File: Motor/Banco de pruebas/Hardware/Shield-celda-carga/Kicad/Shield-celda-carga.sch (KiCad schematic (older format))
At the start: 12 parts, among them J1 Screw_Terminal_01x02, J2 Screw_Terminal_01x03, J3 Conn_01x04, J4 Alimentacion Arduino, K1 Rele 12V-360mW, Q1 BC337, U1 HX711

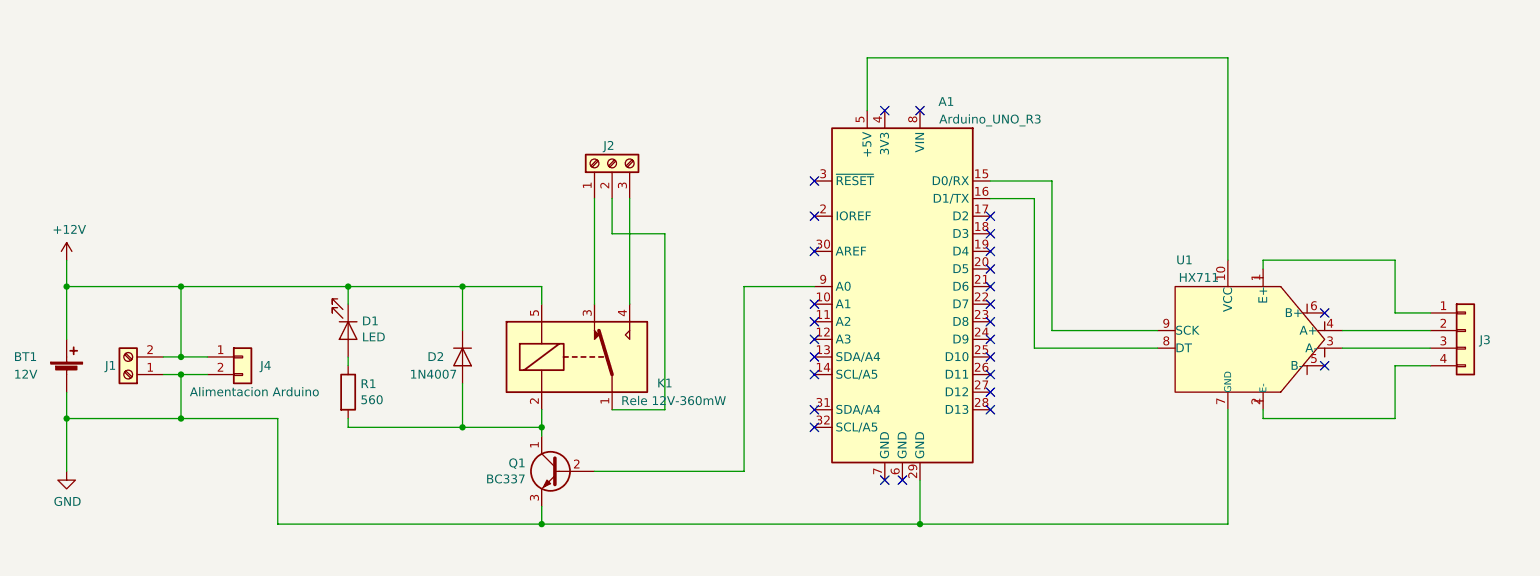
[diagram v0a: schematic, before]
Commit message: Nueva placa Shield-celda-carga
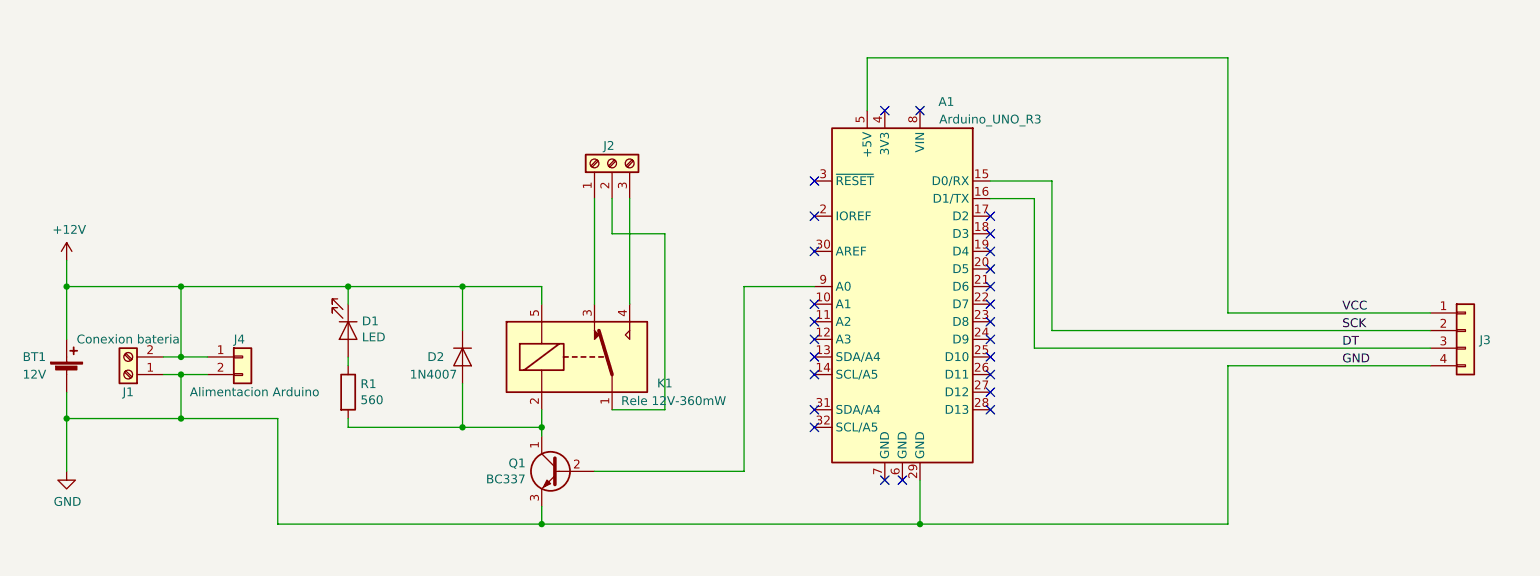
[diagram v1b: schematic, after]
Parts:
- removed U1: HX711, kicad:HX711 module, symbol hx711:HX711
- J1: value Screw_Terminal_01x02 -> Conexion bateria
- J3: footprint Connector_PinHeader_2.54mm:PinHeader_1x05_P2.54mm_Horizontal -> Connector_PinHeader_2.54mm:PinHeader_1x04_P2.54mm_Horizontal
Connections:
- net GND: now also J3.4 (Pin_4)
- net SCK: now reaches A1.15 (D0/RX)
- net SCK: now also J3.2 (Pin_2)
- net DT: now reaches A1.16 (D1/TX)
- net DT: now also J3.3 (Pin_3)
- net VCC: now reaches A1.5 (+5V)
- net VCC: now also J3.1 (Pin_1)
- no-connect marks 28 -> 26
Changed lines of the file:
@@
 $EndComp
-$Comp
-L hx711:HX711 U1
-U 1 1 5E88FDFC
-P 7450 2600
-F 0 "U1" H 7650 3050 50  0000 L CNN
-F 1 "HX711" H 7500 2950 50  0000 L CNN
-F 2 "kicad:HX711 module" H 7500 2950 50  0001 L CNN
-F 3 "http://www.ti.com/lit/ds/symlink/ads1110.pdf" H 7150 2950 50  0001 C CNN
-	1    7450 2600
-	-1   0    0    -1
-$EndComp
-Wire Wire Line
-	7450 3000 7450 3650
-Wire Wire Line
-	7450 2150 7450 1000
 $Comp
 L Connector_Generic:Conn_01x04 J3
@@
 F 0 "J3" H 8880 2496 50  0000 L CNN
 F 1 "Conn_01x04" H 8880 2451 50  0001 L CNN
-F 2 "Connector_PinHeader_2.54mm:PinHeader_1x05_P2.54mm_Horizontal" H 8800 2550 50  0001 C CNN
+F 2 "Connector_PinHeader_2.54mm:PinHeader_1x04_P2.54mm_Horizontal" H 8800 2550 50  0001 C CNN
 F 3 "~" H 8800 2550 50  0001 C CNN
 	1    8800 2550
 	1    0    0    -1
 $EndComp
-Wire Wire Line
-	8100 2550 8600 2550
-Wire Wire Line
-	8600 2650 8100 2650
-Wire Wire Line
-	7650 2200 7650 2150
-Wire Wire Line
-	8400 2450 8600 2450
-Wire Wire Line
-	7650 3000 7650 3050
-Wire Wire Line
-	7650 3050 8400 3050
-Wire Wire Line
-	8400 3050 8400 2750
-Wire Wire Line
-	8400 2750 8600 2750
 $Comp
 L Connector:Screw_Terminal_01x02 J1
 U 1 1 5E898B2F
 P 1200 2800
-F 0 "J1" H 1300 2750 50  0000 C CNN
-F 1 "Screw_Terminal_01x02" H 1118 2566 50  0001 C CNN
+F 0 "J1" H 1200 2900 50  0000 C CNN
+F 1 "Conexion bateria" H 1200 2600 50  0000 C CNN
 F 2 "TerminalBlock_Altech:Altech_AK300_1x02_P5.00mm_45-Degree" H 1200 2800 50  0001 C CNN
 F 3 "~" H 1200 2800 50  0001 C CNN
@@
 U 1 1 5E899902
 P 850 2800
-F 0 "BT1" H 550 2900 50  0000 L CNN
-F 1 "12V" H 550 2800 50  0000 L CNN
+F 0 "BT1" H 600 2900 50  0000 L CNN
+F 1 "12V" H 600 2800 50  0000 L CNN
 F 2 "" V 850 2860 50  0001 C CNN
 F 3 "~" V 850 2860 50  0001 C CNN
@@
 	5400 1000 5400 1300
 Wire Wire Line
-	6350 2650 6350 1800
-Wire Wire Line
 	6350 1800 6100 1800
 Wire Wire Line
-	6350 2650 7050 2650
-Wire Wire Line
 	6100 1700 6450 1700
-Wire Wire Line
-	6450 1700 6450 2550
-Wire Wire Line
-	6450 2550 7050 2550
 Wire Wire Line
 	5700 3400 5700 3650
@@
 	2450 3100 3100 3100
 Connection ~ 3100 3100
-NoConn ~ 8000 2450
-NoConn ~ 8000 2750
 NoConn ~ 5100 1700
 NoConn ~ 5100 1900
@@
 Connection ~ 850  3050
 Wire Wire Line
-	8400 2150 8400 2450
-Wire Wire Line
-	7650 2150 8400 2150
-Wire Wire Line
 	3850 1800 3850 2400
 Wire Wire Line
@@
 U 1 1 5E8DE260
 P 1850 2700
-F 0 "J4" H 1950 2650 50  0000 L CNN
+F 0 "J4" H 1800 2800 50  0000 L CNN
 F 1 "Alimentacion Arduino" H 1550 2500 50  0000 L CNN
 F 2 "Connector_PinHeader_2.54mm:PinHeader_1x02_P2.54mm_Vertical" H 1850 2700 50  0001 C CNN
@@
 Wire Wire Line
 	1500 3050 2050 3050
+Text Label 8100 2550 0    50   ~ 0
+SCK
+Text Label 8100 2650 0    50   ~ 0
+DT
+Text Label 8100 2450 0    50   ~ 0
+VCC
+Text Label 8100 2750 0    50   ~ 0
+GND
+Wire Wire Line
+	6450 1700 6450 2550
+Wire Wire Line
+	6450 2550 8600 2550
+Wire Wire Line
+	6350 1800 6350 2650
+Wire Wire Line
+	6350 2650 8600 2650
+Wire Wire Line
+	7450 1000 7450 2450
+Wire Wire Line
+	7450 2450 8600 2450
+Wire Wire Line
+	7450 2750 7450 3650
+Wire Wire Line
+	7450 2750 8600 2750
 $EndSCHEMATC

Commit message: se modifico shiel-celda-carga la distribucion de pines
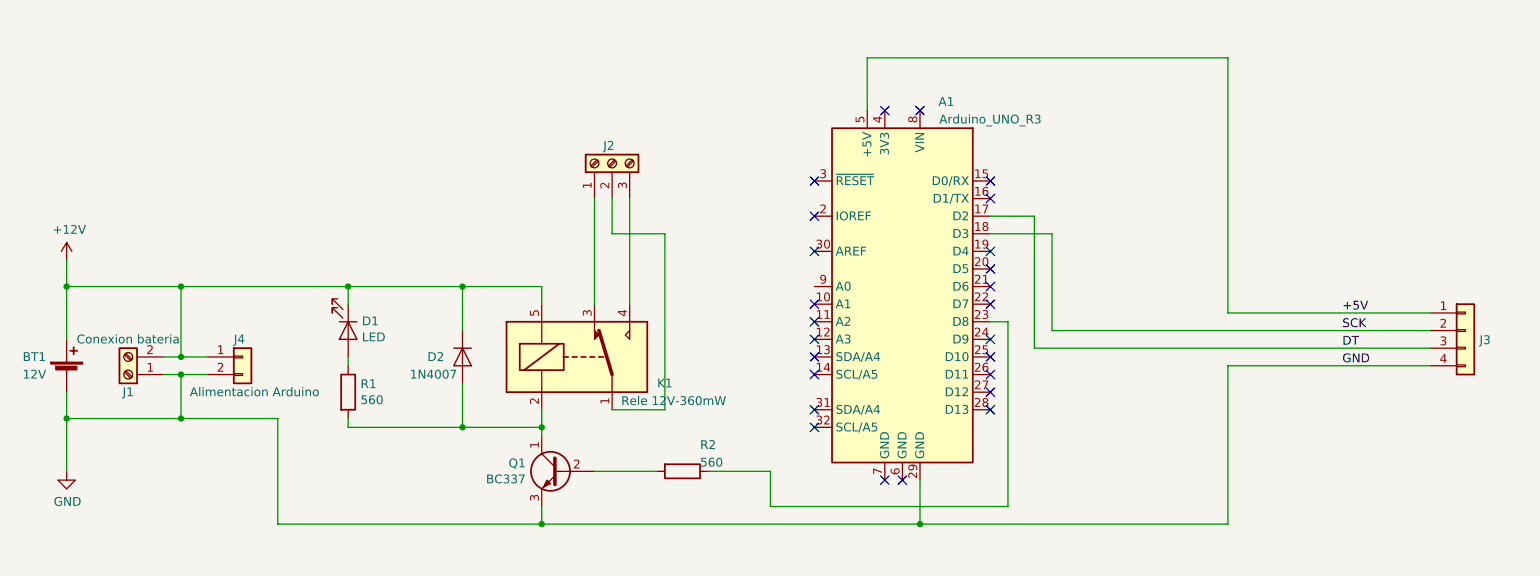
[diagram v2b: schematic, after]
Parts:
- added R2: 560, Resistor_THT:R_Axial_DIN0207_L6.3mm_D2.5mm_P7.62mm_Horizontal, symbol Device:R
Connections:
- net DT: now also A1.17 (D2); no longer A1.16 (D1/TX)
- net SCK: now also A1.18 (D3); no longer A1.15 (D0/RX)
- net at A1.23 (D8): now also R2.1
- net at A1.9 (A0): no longer Q1.2 (B)
- net VCC renamed +5V
- new net: Q1.2 (B), R2.2
- no-connect marks 26 -> 25
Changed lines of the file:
@@
 	5400 1000 5400 1300
-Wire Wire Line
-	6350 1800 6100 1800
-Wire Wire Line
-	6100 1700 6450 1700
 Wire Wire Line
 	5700 3400 5700 3650
@@
 Wire Wire Line
 	5700 3650 7450 3650
-Wire Wire Line
-	5100 2300 4700 2300
-Wire Wire Line
-	4700 2300 4700 3350
-Wire Wire Line
-	4700 3350 3850 3350
 Wire Wire Line
 	850  2900 850  3050
@@
 NoConn ~ 5500 1300
 NoConn ~ 5700 1300
-NoConn ~ 6100 1900
-NoConn ~ 6100 2000
 NoConn ~ 6100 2100
 NoConn ~ 6100 2200
 NoConn ~ 6100 2300
 NoConn ~ 6100 2400
-NoConn ~ 6100 2500
 NoConn ~ 6100 2600
 NoConn ~ 6100 2800
@@
 DT
 Text Label 8100 2450 0    50   ~ 0
-VCC
++5V
 Text Label 8100 2750 0    50   ~ 0
 GND
 Wire Wire Line
-	6450 1700 6450 2550
-Wire Wire Line
 	6450 2550 8600 2550
 Wire Wire Line
-	6350 1800 6350 2650
-Wire Wire Line
 	6350 2650 8600 2650
 Wire Wire Line
@@
 Wire Wire Line
 	7450 2750 8600 2750
+Wire Wire Line
+	6350 1900 6100 1900
+Wire Wire Line
+	6350 1900 6350 2650
+Wire Wire Line
+	6100 2000 6450 2000
+Wire Wire Line
+	6450 2000 6450 2550
+NoConn ~ 6100 1700
+NoConn ~ 6100 1800
+Wire Wire Line
+	4850 3350 4850 3550
+Wire Wire Line
+	4850 3550 6200 3550
+Wire Wire Line
+	6200 3550 6200 2500
+Wire Wire Line
+	6200 2500 6100 2500
+$Comp
+L Device:R R2
+U 1 1 5E9BED75
+P 4350 3350
+F 0 "R2" V 4200 3450 50  0000 L CNN
+F 1 "560" V 4300 3450 50  0000 L CNN
+F 2 "Resistor_THT:R_Axial_DIN0207_L6.3mm_D2.5mm_P7.62mm_Horizontal" V 4280 3350 50  0001 C CNN
+F 3 "~" H 4350 3350 50  0001 C CNN
+	1    4350 3350
+	0    1    1    0
+$EndComp
+Wire Wire Line
+	4850 3350 4500 3350
+Wire Wire Line
+	4200 3350 3850 3350
 $EndSCHEMATC

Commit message: Se agrego un circuito RC en la base del transistor del rele por problemas de ruiido al resetear y se creo la Rev2
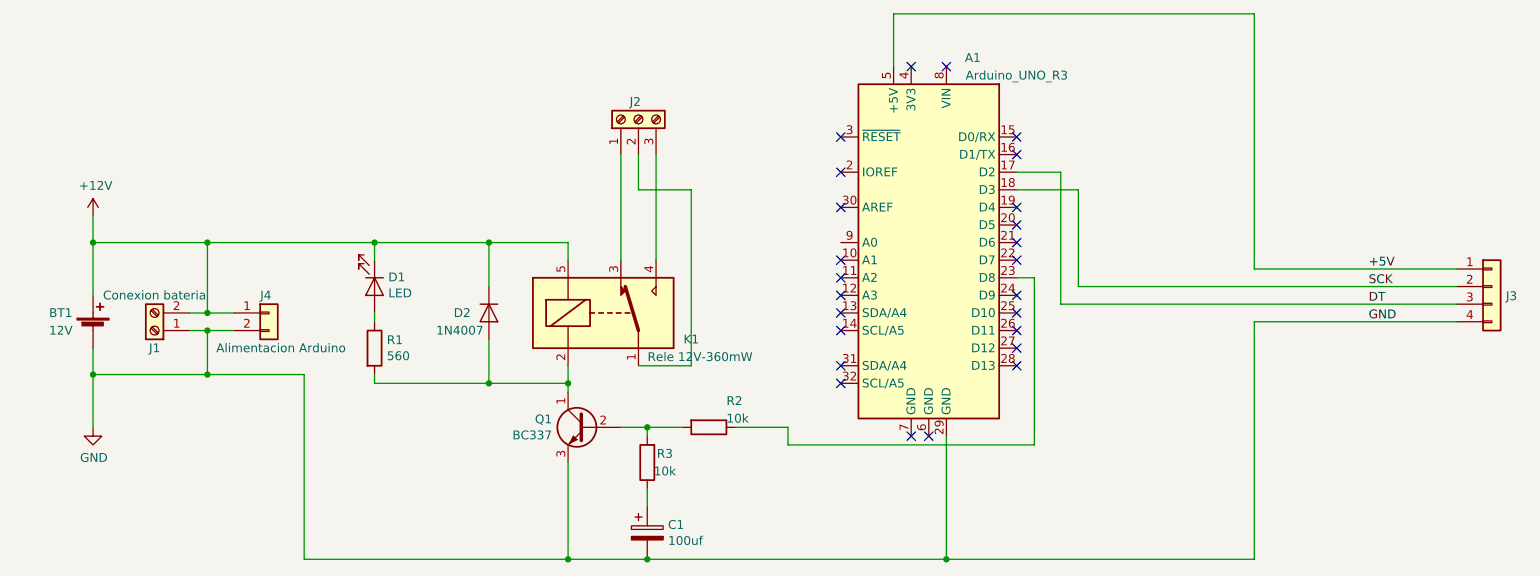
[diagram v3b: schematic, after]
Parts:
- added C1: 100uf, Capacitor_THT:CP_Radial_D6.3mm_P2.50mm, symbol Device:CP
- added R3: 10k, Resistor_THT:R_Axial_DIN0207_L6.3mm_D2.5mm_P7.62mm_Horizontal, symbol Device:R
- R2: value 560 -> 10k
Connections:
- net GND: now also C1.2
- net at Q1.2 (B), R2.2: now also R3.2
- new net: C1.1, R3.1
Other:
- moved on the sheet: A1, BT1, D1, D2, J1, J2, J3, J4, K1, Q1, R1, R2
